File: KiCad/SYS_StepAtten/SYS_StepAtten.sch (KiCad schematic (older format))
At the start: 172 parts

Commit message: Changed to RGB LED
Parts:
- removed D?: LED0, LED_SMD:LED_0805_2012Metric, symbol Device:LED_Small
- removed D?: LED1, LED_SMD:LED_0805_2012Metric, symbol Device:LED_Small
- removed D?: LED2, LED_SMD:LED_0805_2012Metric, symbol Device:LED_Small
- added D?: LED_RGBA, RGB_LED_1.6x1.6x0:RGB_LED_1.6x1.6x0.6, symbol Device:LED_RGBA
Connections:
- wire segments 620 -> 616
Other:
- moved on the sheet: R?
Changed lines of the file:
@@
-$EndComp
-$Comp
-L Device:LED_Small D?
-U 1 1 633AEB6A
-P 2650 6400
-F 0 "D?" H 2650 6195 50  0000 C CNN
-F 1 "LED0" H 2650 6286 50  0000 C CNN
-F 2 "LED_SMD:LED_0805_2012Metric" V 2650 6400 50  0001 C CNN
-F 3 "~" V 2650 6400 50  0001 C CNN
-	1    2650 6400
-	-1   0    0    1
-$EndComp
-$Comp
-L Device:LED_Small D?
-U 1 1 633B113E
-P 2650 6800
-F 0 "D?" H 2650 6595 50  0000 C CNN
-F 1 "LED1" H 2650 6686 50  0000 C CNN
-F 2 "LED_SMD:LED_0805_2012Metric" V 2650 6800 50  0001 C CNN
-F 3 "~" V 2650 6800 50  0001 C CNN
-	1    2650 6800
-	-1   0    0    1
-$EndComp
-$Comp
-L Device:LED_Small D?
-U 1 1 633B15F1
-P 2650 7250
-F 0 "D?" H 2650 7045 50  0000 C CNN
-F 1 "LED2" H 2650 7136 50  0000 C CNN
-F 2 "LED_SMD:LED_0805_2012Metric" V 2650 7250 50  0001 C CNN
-F 3 "~" V 2650 7250 50  0001 C CNN
-	1    2650 7250
-	-1   0    0    1
 $EndComp
 $Comp
 L Device:R_Small R?
 U 1 1 633B1B09
-P 3150 6400
-F 0 "R?" V 2954 6400 50  0000 C CNN
-F 1 "1K" V 3045 6400 50  0000 C CNN
-F 2 "Resistor_SMD:R_0603_1608Metric" H 3150 6400 50  0001 C CNN
-F 3 "~" H 3150 6400 50  0001 C CNN
-	1    3150 6400
+P 2650 6600
+F 0 "R?" V 2600 6750 50  0000 C CNN
+F 1 "1K" V 2600 6450 50  0000 C CNN
+F 2 "Resistor_SMD:R_0603_1608Metric" H 2650 6600 50  0001 C CNN
+F 3 "~" H 2650 6600 50  0001 C CNN
+	1    2650 6600
 	0    1    1    0
 $EndComp
@@
 L Device:R_Small R?
 U 1 1 633B2379
-P 3150 6800
-F 0 "R?" V 2954 6800 50  0000 C CNN
-F 1 "1K" V 3045 6800 50  0000 C CNN
-F 2 "Resistor_SMD:R_0603_1608Metric" H 3150 6800 50  0001 C CNN
-F 3 "~" H 3150 6800 50  0001 C CNN
-	1    3150 6800
+P 2650 6800
+F 0 "R?" V 2600 6950 50  0000 C CNN
+F 1 "1K" V 2600 6650 50  0000 C CNN
+F 2 "Resistor_SMD:R_0603_1608Metric" H 2650 6800 50  0001 C CNN
+F 3 "~" H 2650 6800 50  0001 C CNN
+	1    2650 6800
 	0    1    1    0
 $EndComp
@@
 L Device:R_Small R?
 U 1 1 633B26FC
-P 3150 7250
-F 0 "R?" V 2954 7250 50  0000 C CNN
-F 1 "1K" V 3045 7250 50  0000 C CNN
-F 2 "Resistor_SMD:R_0603_1608Metric" H 3150 7250 50  0001 C CNN
-F 3 "~" H 3150 7250 50  0001 C CNN
-	1    3150 7250
+P 2650 7000
+F 0 "R?" V 2600 7150 50  0000 C CNN
+F 1 "1K" V 2600 6850 50  0000 C CNN
+F 2 "Resistor_SMD:R_0603_1608Metric" H 2650 7000 50  0001 C CNN
+F 3 "~" H 2650 7000 50  0001 C CNN
+	1    2650 7000
 	0    1    1    0
 $EndComp
-$Comp
-L power:GND #PWR?
-U 1 1 633B2BA6
-P 3450 6500
-F 0 "#PWR?" H 3450 6250 50  0001 C CNN
-F 1 "GND" H 3455 6327 50  0000 C CNN
-F 2 "" H 3450 6500 50  0001 C CNN
-F 3 "" H 3450 6500 50  0001 C CNN
-	1    3450 6500
-	1    0    0    -1
-$EndComp
-$Comp
-L power:GND #PWR?
-U 1 1 633B37B4
-P 3450 6950
-F 0 "#PWR?" H 3450 6700 50  0001 C CNN
-F 1 "GND" H 3455 6777 50  0000 C CNN
-F 2 "" H 3450 6950 50  0001 C CNN
-F 3 "" H 3450 6950 50  0001 C CNN
-	1    3450 6950
-	1    0    0    -1
-$EndComp
-$Comp
-L power:GND #PWR?
-U 1 1 633B3B80
-P 3450 7400
-F 0 "#PWR?" H 3450 7150 50  0001 C CNN
-F 1 "GND" H 3455 7227 50  0000 C CNN
-F 2 "" H 3450 7400 50  0001 C CNN
-F 3 "" H 3450 7400 50  0001 C CNN
-	1    3450 7400
-	1    0    0    -1
-$EndComp
-Wire Wire Line
-	3450 7400 3450 7250
-Wire Wire Line
-	3450 7250 3250 7250
-Wire Wire Line
-	3250 6800 3450 6800
-Wire Wire Line
-	3450 6800 3450 6950
-Wire Wire Line
-	3250 6400 3450 6400
-Wire Wire Line
-	3450 6400 3450 6500
-Wire Wire Line
-	3050 6400 2750 6400
-Wire Wire Line
-	2750 6800 3050 6800
-Wire Wire Line
-	3050 7250 2750 7250
-Text Label 2400 6400 2    50   ~ 0
+Text Label 2250 6600 0    50   ~ 0
 led0
-Text Label 2400 7250 2    50   ~ 0
+Text Label 2250 7000 0    50   ~ 0
 led2
-Wire Wire Line
-	2400 6400 2550 6400
-Text Label 2400 6800 2    50   ~ 0
+Text Label 2250 6800 0    50   ~ 0
 led1
-Wire Wire Line
-	2400 6800 2550 6800
-Wire Wire Line
-	2400 7250 2550 7250
 Wire Wire Line
 	2450 3950 2450 3750
@@
 	1    0    0    -1
 $EndComp
+$Comp
+L Device:LED_RGBA D?
+U 1 1 60680B6C
+P 3050 6800
+F 0 "D?" H 3050 7297 50  0000 C CNN
+F 1 "LED_RGBA" H 3050 7206 50  0000 C CNN
+F 2 "RGB_LED_1.6x1.6x0:RGB_LED_1.6x1.6x0.6" H 3050 6750 50  0001 C CNN
+F 3 "~" H 3050 6750 50  0001 C CNN
+	1    3050 6800
+	1    0    0    -1
+$EndComp
+Wire Wire Line
+	2750 6600 2850 6600
+Wire Wire Line
+	2250 6600 2550 6600
+Wire Wire Line
+	2250 6800 2550 6800
+Wire Wire Line
+	2250 7000 2550 7000
+Wire Wire Line
+	2750 7000 2850 7000
+Wire Wire Line
+	2850 6800 2750 6800
+Wire Wire Line
+	3250 6800 3400 6800
+Wire Wire Line
+	3400 6800 3400 6750
+$Comp
+L power:+3V3 #PWR?
+U 1 1 60CF9034
+P 3400 6750
+F 0 "#PWR?" H 3400 6600 50  0001 C CNN
+F 1 "+3V3" H 3415 6923 50  0000 C CNN
+F 2 "" H 3400 6750 50  0001 C CNN
+F 3 "" H 3400 6750 50  0001 C CNN
+	1    3400 6750
+	1    0    0    -1
+$EndComp

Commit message: Pulled in new RCA_Stereo Symbol, Made sure L/R Channels are correct
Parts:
- R? (x10): footprint (none) -> Resistor_SMD:R_0603_1608Metric
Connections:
- net AGND_L: now also J?.1
- net AGND_R: now also J?.3
- net RCA1_GNDL: now also J?.1
- net RCA1_GNDR: now also J?.3
- net RCA1_L: now also J?.2
- net RCA1_R: now also J?.4
- net RCA2_GNDL: now also J?.1
- net RCA2_GNDR: now also J?.3
- net RCA2_L: now also J?.2
- net RCA2_R: now also J?.4
- net at R?.1, R?.1: now also J?.4
- net at R?.1, R?.1: now also J?.2
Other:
- moved on the sheet: J?, R?

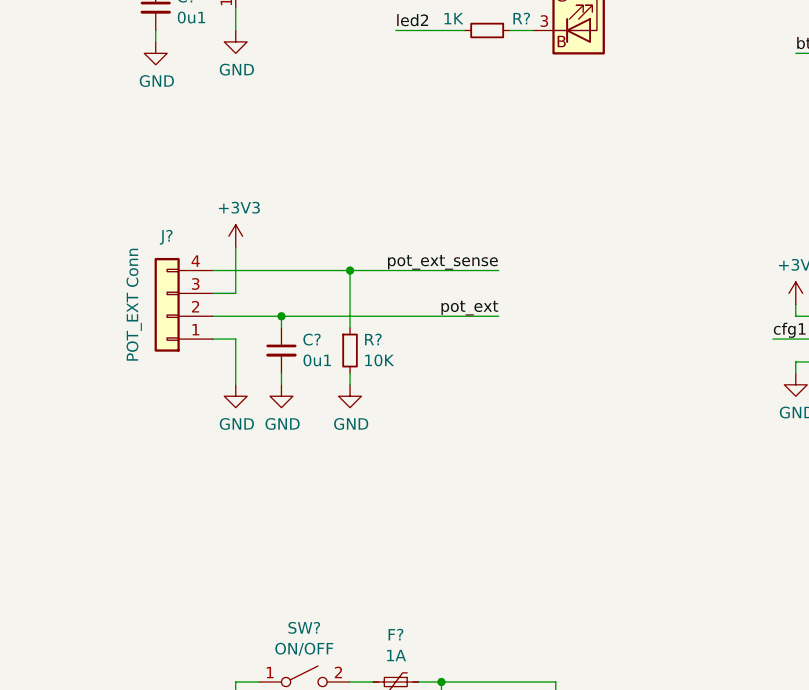
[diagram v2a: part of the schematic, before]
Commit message: Added ESD protection to external poti interface
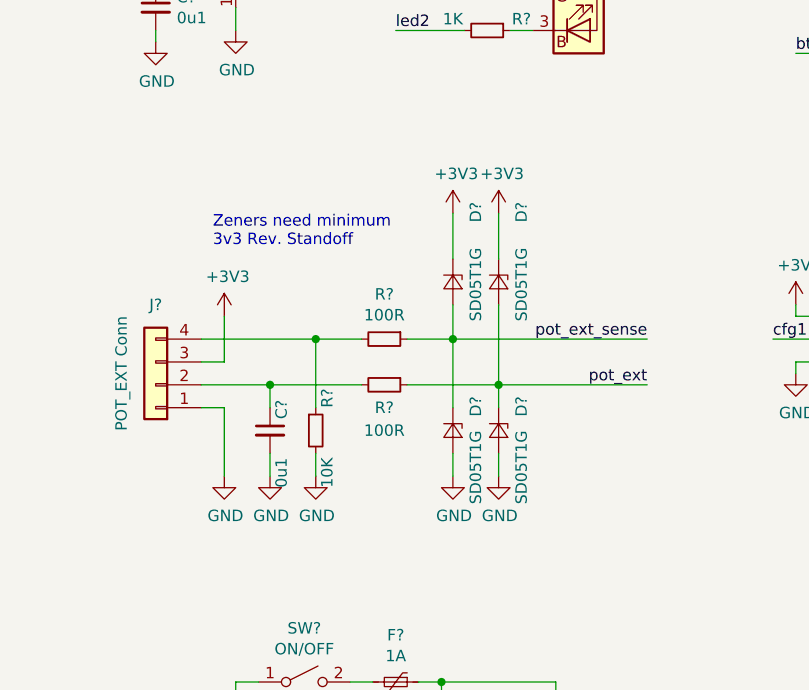
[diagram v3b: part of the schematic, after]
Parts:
- added D? (x4): SD05T1G, Diode_SMD:D_SOD-323, symbol Device:D_Zener_Small
- added R? (x2): 100R, symbol Device:R_Small
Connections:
- net +3V3: now also D?.1 (K), D?.1 (K)
- net GND: now also D?.2 (A), D?.2 (A)
- net pot_ext: now also D?.1 (K), D?.2 (A), R?.1; no longer C?.1, J?.2 (Pin_2)
- net pot_ext_sense: now also D?.1 (K), D?.2 (A), R?.1; no longer J?.4 (Pin_4), R?.1
- new net: J?.4 (Pin_4), R?.1, R?.2
- new net: C?.1, J?.2 (Pin_2), R?.2
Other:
- note added: "Zeners need minimum\n3v3 Rev. Standoff"
- moved on the sheet: C?, J?, R?

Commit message: Added Mounting Hole Footprint
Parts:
- H? (x2): footprint (none) -> MountingHole_4.3mm_M4_ReducedSize:MountingHole_4.3mm_M4_Pad_Via
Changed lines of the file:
@@
 F 0 "H?" H 10800 9949 50  0000 L CNN
 F 1 "MountingHole 1" H 10800 9858 50  0001 L CNN
-F 2 "" H 10700 9900 50  0001 C CNN
+F 2 "MountingHole_4.3mm_M4_ReducedSize:MountingHole_4.3mm_M4_Pad_Via" H 10700 9900 50  0001 C CNN
 F 3 "~" H 10700 9900 50  0001 C CNN
 	1    10700 9900
@@
 F 0 "H?" H 9950 9949 50  0000 L CNN
 F 1 "MH 1" H 9950 9858 50  0001 L CNN
-F 2 "" H 9850 9900 50  0001 C CNN
+F 2 "MountingHole_4.3mm_M4_ReducedSize:MountingHole_4.3mm_M4_Pad_Via" H 9850 9900 50  0001 C CNN
 F 3 "~" H 9850 9900 50  0001 C CNN
 	1    9850 9900

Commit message: Annotated Schematic, Added last few footprints
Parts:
- J10, J11: renamed from J?; footprint (none) -> Connector_PinSocket_2.54mm:PinSocket_1x03_P2.54mm_Vertical
- R2, R3: renamed from R?; footprint (none) -> Resistor_SMD:R_0603_1608Metric
- gave numbers to parts that had none: 143
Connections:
- net +5V_A: now also K2.1, K3.1, K4.1, K5.1, K6.1, K7.1; no longer K2.1, K3.1, K4.1, K5.1, K6.1, K7.1
- net +5V_B: now also K10.1, K11.1, K12.1, K13.1, K14.1, K8.1, K9.1; no longer K10.1, K11.1, K12.1, K13.1, K14.1, K8.1, K9.1
- net AGND_L: now also K14.9, K3.8; no longer K14.2, K3.3
- net AGND_R: now also K14.2, K3.3; no longer K14.9, K3.8
- net AUX1_L: now also K5.9; no longer K5.2
- net AUX1_R: now also K5.2; no longer K5.9
- net AUX2_L: now also K5.7; no longer K5.4
- net AUX2_R: now also K5.4; no longer K5.7
- net RCA1_GNDL: now also K2.9; no longer K2.2
- net RCA1_GNDR: now also K2.2; no longer K2.9
- net RCA1_L: now also K4.9; no longer K4.2
- net RCA1_R: now also K4.2; no longer K4.9
- net RCA2_GNDL: now also K2.7; no longer K2.4
- net RCA2_GNDR: now also K2.4; no longer K2.7
- net RCA2_L: now also K4.7; no longer K4.4
- net RCA2_R: now also K4.4; no longer K4.7
- net at R12.1, R16.2: now also K7.3, K8.4; no longer K7.8, K8.7
- net at R11.1, R15.2: now also K7.8, K8.7; no longer K7.3, K8.4
- net at R9.2: now also K7.9; no longer K7.2
- net at R10.2: now also K7.2; no longer K7.9
- net at R16.1, R21.2: now also K8.3, K9.4; no longer K8.8, K9.7
- net at R15.1, R20.2: now also K8.8, K9.7; no longer K8.3, K9.4
- net at R13.2: now also K8.9; no longer K8.2
- net at R14.2: now also K8.2; no longer K8.9
- net at R21.1, R25.2: now also K10.4, K9.3; no longer K10.7, K9.8
- net at R20.1, R24.2: now also K10.7, K9.8; no longer K10.4, K9.3
- net at R18.2: now also K9.9; no longer K9.2
- net at R19.2: now also K9.2; no longer K9.9
- net at R25.1, R29.2: now also K10.3, K11.4; no longer K10.8, K11.7
- net at R24.1, R28.2: now also K10.8, K11.7; no longer K10.3, K11.4
- net at R22.2: now also K10.9; no longer K10.2
- net at R23.2: now also K10.2; no longer K10.9
- net at R29.1, R33.2: now also K11.3, K12.4; no longer K11.8, K12.7
- net at R28.1, R32.2: now also K11.8, K12.7; no longer K11.3, K12.4
- net at R26.2: now also K11.9; no longer K11.2
- net at R27.2: now also K11.2; no longer K11.9
- net at R33.1, R43.2: now also K12.3, K13.4; no longer K12.8, K13.7
- net at R32.1, R42.2: now also K12.8, K13.7; no longer K12.3, K13.4
- net at R30.2: now also K12.9; no longer K12.2
- net at R31.2: now also K12.2; no longer K12.9
- net at R38.2: now also K13.9; no longer K13.2
- net at R39.2: now also K13.2; no longer K13.9
- net at D13.2 (A), Q4.3 (D): now also K4.10; no longer K4.10
- net at D11.2 (A), Q2.3 (D): now also K2.10; no longer K2.10
- net at D12.2 (A), Q3.3 (D): now also K3.10; no longer K3.10
- net at R49.2: now also K14.3; no longer K14.8
- net at R48.2: now also K14.8; no longer K14.3
- net at D14.2 (A), Q5.3 (D): now also K5.10; no longer K5.10
- net at D15.2 (A), Q6.3 (D): now also K6.10; no longer K6.10
- net at D16.2 (A), Q7.3 (D): now also K7.10; no longer K7.10
- net at D17.2 (A), Q8.3 (D): now also K8.10; no longer K8.10
- net at D18.2 (A), Q9.3 (D): now also K9.10; no longer K9.10
- net at D19.2 (A), Q10.3 (D): now also K10.10; no longer K10.10
- net at D20.2 (A), Q11.3 (D): now also K11.10; no longer K11.10
- net at D21.2 (A), Q12.3 (D): now also K12.10; no longer K12.10
- net at D22.2 (A), Q13.3 (D): now also K13.10; no longer K13.10
- net at D23.2 (A), Q14.3 (D): now also K14.10; no longer K14.10
- new net: K6.3, K7.4, R12.2
- new net: K6.8, K7.7, R11.2
- new net: K13.3, K14.4, R43.1
- new net: K13.8, K14.7, R42.1
- new net: K1.3, K3.4, K3.7
- new net: K2.8, K3.9
- new net: K2.3, K3.2
- new net: K4.8, K6.9
- new net: K4.3, K6.2
- new net: K5.8, K6.7
- new net: K5.3, K6.4
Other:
- moved on the sheet: K1B, K1C

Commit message: Layout1
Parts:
- removed C6, C7: 22pf, Capacitor_SMD:C_0603_1608Metric, symbol Device:C_Small
- removed Y1: 8Mhz, Crystal:Crystal_SMD_EuroQuartz_MJ-4Pin_5.0x3.2mm, symbol Device:Crystal_GND24
- J10, J11: footprint Connector_PinSocket_2.54mm:PinSocket_1x03_P2.54mm_Vertical -> Connector_PinHeader_2.54mm:PinHeader_1x03_P2.54mm_Vertical
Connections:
- net AUX1_GND: now also K1.9; no longer K1.2
- net AUX2_GND: now also K1.7; no longer K1.4
- net at K1.8: now also K3.4, K3.7
- net PF0_OSC: no longer names the net of U4.2 (PF0)
- net PF1_OSC: no longer names the net of U4.3 (PF1)
- now unconnected: K1.3
- no-connect marks 12 -> 14
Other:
- moved on the sheet: K1B, K1C
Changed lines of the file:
@@
 	9700 6300 9700 6400
 $Comp
-L Device:Crystal_GND24 Y1
-U 1 1 5ED94C61
-P 6600 6850
-F 0 "Y1" V 6500 7050 50  0000 L CNN
-F 1 "8Mhz" V 6700 7050 50  0000 L CNN
-F 2 "Crystal:Crystal_SMD_EuroQuartz_MJ-4Pin_5.0x3.2mm" H 6600 6850 50  0001 C CNN
-F 3 "~" H 6600 6850 50  0001 C CNN
-	1    6600 6850
-	0    -1   -1   0
-$EndComp
-$Comp
-L Device:C_Small C6
-U 1 1 5ED96D0F
-P 6350 6500
-F 0 "C6" V 6250 6600 50  0000 C CNN
-F 1 "22pf" V 6450 6500 50  0000 C CNN
-F 2 "Capacitor_SMD:C_0603_1608Metric" H 6350 6500 50  0001 C CNN
-F 3 "~" H 6350 6500 50  0001 C CNN
-	1    6350 6500
-	0    -1   -1   0
-$EndComp
-Wire Wire Line
-	6450 6500 6600 6500
-$Comp
-L Device:C_Small C7
-U 1 1 5EDF5E0B
-P 6350 7150
-F 0 "C7" V 6250 7050 50  0000 C CNN
-F 1 "22pf" V 6500 7150 50  0000 C CNN
-F 2 "Capacitor_SMD:C_0603_1608Metric" H 6350 7150 50  0001 C CNN
-F 3 "~" H 6350 7150 50  0001 C CNN
-	1    6350 7150
-	0    1    1    0
-$EndComp
-Wire Wire Line
-	6450 7150 6600 7150
-Wire Wire Line
-	6250 7150 6100 7150
-$Comp
-L power:GND #PWR0105
-U 1 1 5EE55B11
-P 6100 7150
-F 0 "#PWR0105" H 6100 6900 50  0001 C CNN
-F 1 "GND" V 6105 7022 50  0000 R CNN
-F 2 "" H 6100 7150 50  0001 C CNN
-F 3 "" H 6100 7150 50  0001 C CNN
-	1    6100 7150
-	0    1    1    0
-$EndComp
-$Comp
-L power:GND #PWR0106
-U 1 1 5EE55CC3
-P 6100 6500
-F 0 "#PWR0106" H 6100 6250 50  0001 C CNN
-F 1 "GND" V 6105 6372 50  0000 R CNN
-F 2 "" H 6100 6500 50  0001 C CNN
-F 3 "" H 6100 6500 50  0001 C CNN
-	1    6100 6500
-	0    1    1    0
-$EndComp
-Wire Wire Line
-	6100 6500 6250 6500
-Connection ~ 6600 6500
-Connection ~ 6600 7150
-$Comp
 L Regulator_Linear:LM317_3PinPackage U1
 U 1 1 5EF1F50C
@@
 Wire Wire Line
 	10450 8150 10200 8150
-Wire Wire Line
-	6600 7150 6600 7000
-Wire Wire Line
-	6600 6700 6600 6500
-Text Label 7000 7150 2    50   ~ 0
-PF0_OSC
-Text Label 7000 6500 2    50   ~ 0
-PF1_OSC
-Wire Wire Line
-	7000 6500 6600 6500
-Wire Wire Line
-	7000 7150 6600 7150
-Text Label 8700 7650 0    50   ~ 0
-PF0_OSC
-Text Label 8700 7750 0    50   ~ 0
-PF1_OSC
-Wire Wire Line
-	8700 7750 9100 7750
-Wire Wire Line
-	9100 7650 8700 7650
 $Comp
 L Device:R_Small R17
@@
 L Panasonic_TQ2SA:TQ2SA-Multi K1
 U 2 1 5E9A47B4
-P 2700 1650
-F 0 "K1" H 2900 1600 50  0000 C CNN
-F 1 "TQ2SA" H 2700 1800 50  0000 C CNN
-F 2 "Panasonic_TQ2SA:Panasonic_TQ2SA" H 2500 1700 50  0001 C CNN
-F 3 "" H 2500 1700 50  0001 C CNN
-	2    2700 1650
-	1    0    0    -1
-$EndComp
-$Comp
-L Panasonic_TQ2SA:TQ2SA-Multi K1
-U 3 1 5E9985D7
 P 2700 2050
 F 0 "K1" H 2900 2000 50  0000 C CNN
@@
 F 2 "Panasonic_TQ2SA:Panasonic_TQ2SA" H 2500 2100 50  0001 C CNN
 F 3 "" H 2500 2100 50  0001 C CNN
-	3    2700 2050
+	2    2700 2050
+	1    0    0    -1
+$EndComp
+$Comp
+L Panasonic_TQ2SA:TQ2SA-Multi K1
+U 3 1 5E9985D7
+P 2700 1650
+F 0 "K1" H 2900 1600 50  0000 C CNN
+F 1 "TQ2SA" H 2700 1800 50  0000 C CNN
+F 2 "Panasonic_TQ2SA:Panasonic_TQ2SA" H 2500 1700 50  0001 C CNN
+F 3 "" H 2500 1700 50  0001 C CNN
+	3    2700 1650
 	1    0    0    -1
 $EndComp
@@
 $Comp
 L Panasonic_TQ2SA:TQ2SA-Multi K7
-U 1 1 5F2C35E0
-P 7150 3750
-F 0 "K7" H 7150 3650 50  0000 C CNN
-F 1 "TQ2SA" H 7150 3900 50  0000 C CNN
-F 2 "Panasonic_TQ2SA:Panasonic_TQ2SA" H 6950 3800 50  0001 C CNN
-F 3 "" H 6950 3800 50  0001 C CNN
-	1    7150 3750
-	1    0    0    -1
-$EndComp
-$Comp
-L Panasonic_TQ2SA:TQ2SA-Multi K7
 U 2 1 5F2C35E6
 P 7150 2800
@@
 Wire Wire Line
 	5800 1800 6100 1800
-Text Label 4400 2000 0    50   ~ 0
-RCA1_L
 Text Label 4400 1900 0    50   ~ 0
 RCA2_L
@@
 F 0 "J10" H 14730 8842 50  0000 L CNN
 F 1 "RCA1 GND JMP" H 14730 8751 50  0000 L CNN
-F 2 "Connector_PinSocket_2.54mm:PinSocket_1x03_P2.54mm_Vertical" H 14650 8800 50  0001 C CNN
+F 2 "Connector_PinHeader_2.54mm:PinHeader_1x03_P2.54mm_Vertical" H 14650 8800 50  0001 C CNN
 F 3 "~" H 14650 8800 50  0001 C CNN
 	1    14650 8800
@@
 F 0 "J11" H 14730 9392 50  0000 L CNN
 F 1 "RCA2 GND JMP" H 14730 9301 50  0000 L CNN
-F 2 "Connector_PinSocket_2.54mm:PinSocket_1x03_P2.54mm_Vertical" H 14650 9350 50  0001 C CNN
+F 2 "Connector_PinHeader_2.54mm:PinHeader_1x03_P2.54mm_Vertical" H 14650 9350 50  0001 C CNN
 F 3 "~" H 14650 9350 50  0001 C CNN
 	1    14650 9350
@@
 Wire Notes Line
 	6300 2450 6300 2000
+$Comp
+L Panasonic_TQ2SA:TQ2SA-Multi K7
+U 1 1 5F2C35E0
+P 7150 3750
+F 0 "K7" H 7150 3650 50  0000 C CNN
+F 1 "TQ2SA" H 7150 3900 50  0000 C CNN
+F 2 "Panasonic_TQ2SA:Panasonic_TQ2SA" H 6950 3800 50  0001 C CNN
+F 3 "" H 6950 3800 50  0001 C CNN
+	1    7150 3750
+	1    0    0    -1
+$EndComp
+Text Label 4400 2000 0    50   ~ 0
+RCA1_L
+NoConn ~ 9100 7650
+NoConn ~ 9100 7750
 $EndSCHEMATC
